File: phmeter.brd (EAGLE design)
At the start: 132.7 x 36.2 mm, 29 parts, among them IC1 ICL7660CPA, IC3 TL082P, J2 BNCPTH, Q1 12MHz, U1 328P

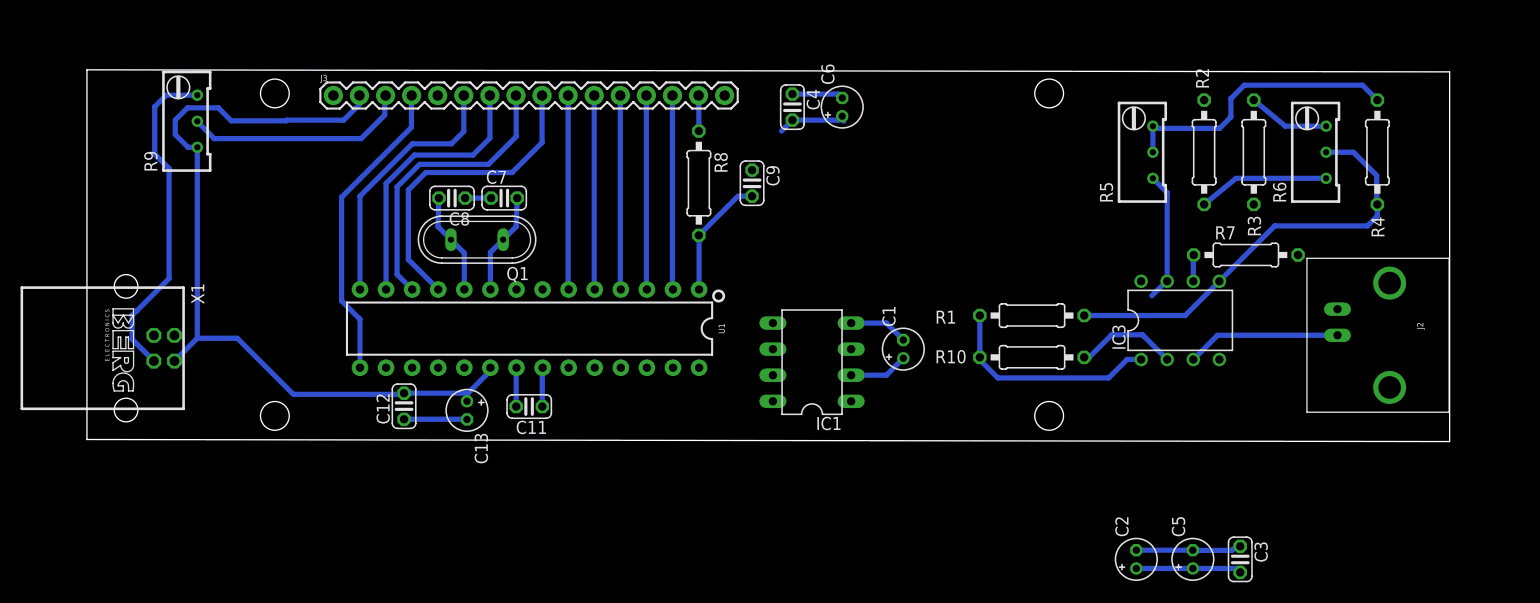
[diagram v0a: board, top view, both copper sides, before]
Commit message: Ended PCB design
Generated PCB and it's pdf file. Ready to print.
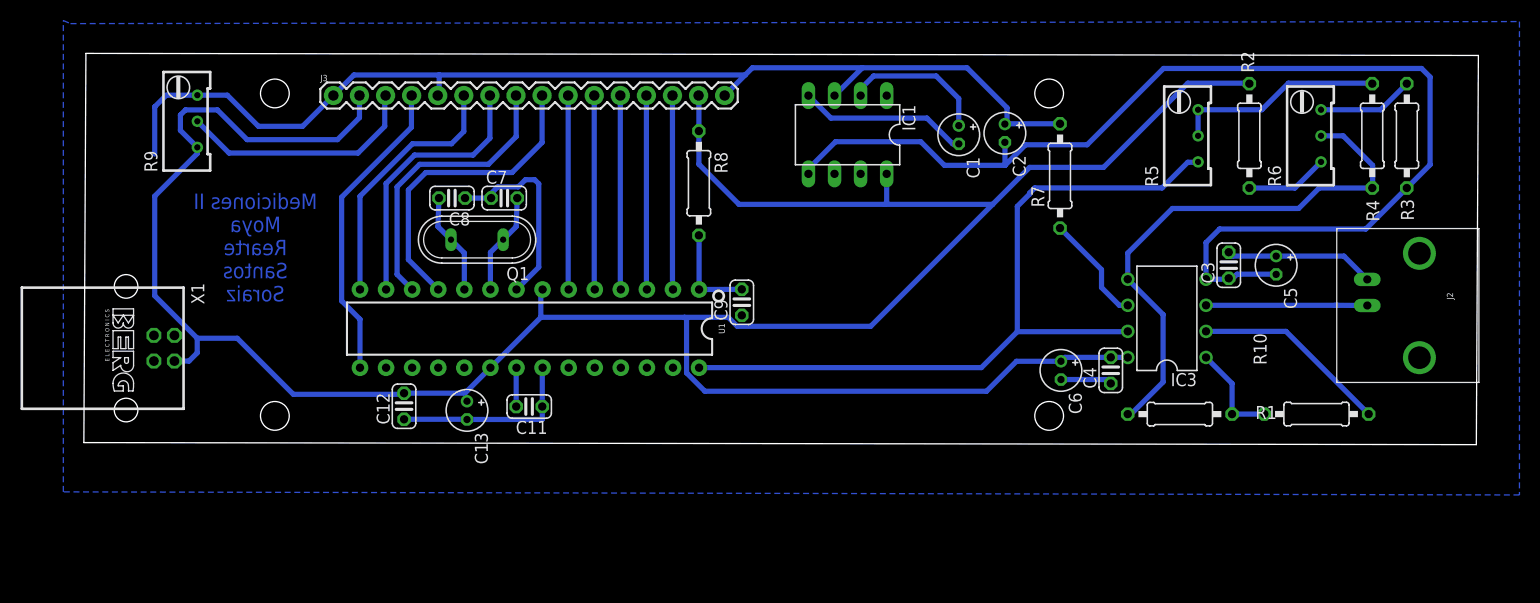
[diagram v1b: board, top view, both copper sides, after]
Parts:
- moved C2 43.4 mm to (89.4, 29.8), turned to 270 degrees
- moved C4 40.2 mm to (99.7, 6.73), turned to 90 degrees
- moved C6 33.3 mm to (94.8, 6.73), turned to 270 degrees
- moved C5 29.8 mm to (115.8, 17.0), turned to 270 degrees
- moved C3 28.7 mm to (111.2, 17.0), turned to 90 degrees
- moved R10 28.2 mm to (119.7, 2.48)
- moved IC1 22.4 mm to (74.1, 29.7), turned to 180 degrees
- moved C1 21.6 mm to (84.9, 29.7), turned to 270 degrees
- moved R7 19.7 mm to (94.8, 25.7), turned to 90 degrees
- moved R1 17.3 mm to (106.4, 2.47), turned to 0 degrees
- moved R3 15.0 mm to (128.5, 29.6)
- moved C9 11.6 mm to (63.8, 13.4), turned to 90 degrees
- moved R2 4.68 mm to (113.2, 29.6)
- moved R5 4.68 mm to (106.9, 29.6)
- moved J2 4.10 mm to (124.7, 13.1)
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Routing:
- net VCC: track 90.0 -> 263.1 mm
- net GND: track 60.4 -> 166.7 mm
- net -VCC: track 10.3 -> 113.7 mm
- net V_ADC: track 12.7 -> 74.9 mm
- net N$1: track 21.5 -> 9.71 mm
- net V_OFFSET: track 42.4 -> 53.6 mm
- net N$5: track 5.76 -> 16.6 mm
- net N$23: track 10.1 -> 19.2 mm
- net N$2: track 5.76 -> 14.3 mm
- net N$4: track 2.58 -> 10.7 mm
- net N$3: track 27.9 -> 20.6 mm
- net N$7: track 12.8 -> 8.03 mm
- net N$12: track 12.1 -> 9.45 mm
- net N$10: track 21.9 -> 23.7 mm
- net N$6: track 7.96 -> 9.41 mm
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- added copper zone on layer 16, net GND
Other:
- board size 132.7 x 36.2 mm -> 135.8 x 38.1 mm
- board text added: "Mediciones II Moya Rearte Santos Soraiz"

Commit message: Finished Board Design
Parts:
- removed C9: 100nF, resistor:C025-024X044
- removed R5: 10k, rcl:RTRIM64W
- removed R6: (no value), rcl:RTRIM64W
- added GAIN: 10k, rcl:RTRIM64W
- added OFFSET: (no value), rcl:RTRIM64W
- moved R3 3.84 mm to (126.1, 26.6)
- moved R4 3.84 mm to (122.8, 26.6)
- moved R2 3.84 mm to (110.8, 26.6)
- moved C5 2.75 mm to (118.1, 15.5)
- moved C3 2.75 mm to (113.5, 15.5)
- moved J2 2.71 mm to (124.5, 10.3)
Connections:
- net GND: no longer C9.1
- net N$12: no longer C9.2
- net N$3: now also GAIN.2, GAIN.3; no longer R5.2, R5.3
- net N$6: now also OFFSET.3; no longer R6.3
- net N$7: now also OFFSET.1; no longer R6.1
- net V_ADC: now also GAIN.1, U1.24; no longer R5.1, U1.28
- net V_OFFSET: now also OFFSET.2; no longer R6.2
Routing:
- net GND: track 166.7 -> 131.9 mm
- net V_ADC: track 74.9 -> 82.9 mm
- net VCC: track 263.1 -> 255.2 mm
- net -VCC: track 113.7 -> 106.3 mm
- net N$12: track 9.45 -> 5.29 mm
- net V_OFFSET: track 53.6 -> 49.9 mm
- net RS: track 30.1 -> 31.7 mm
- net N$10: track 23.7 -> 22.8 mm
- net N$22: track 16.0 -> 16.6 mm
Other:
- outline, holes or cut-outs redrawn
